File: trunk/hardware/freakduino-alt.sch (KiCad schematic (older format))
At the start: 10 parts, among them U6 ATMEGA328-QFP32

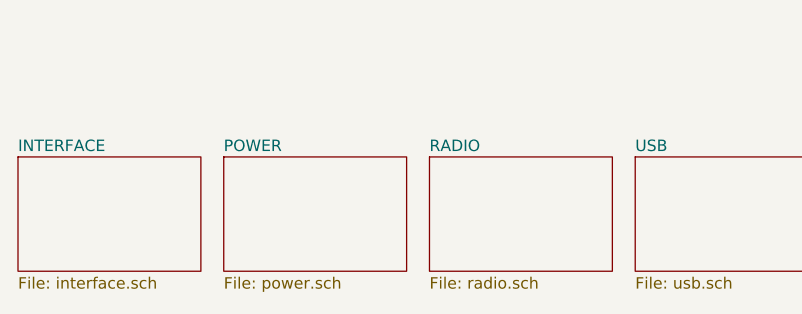
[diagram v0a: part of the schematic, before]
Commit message: CHANGING to -ALT files form this point onwards ...
Due to a number of changes from the original Freakduino design, I'm now
continuing my design in the freakduino-alt project, leaving a copy of the 
original work in the files without -alt.

The single shre/ folder (freakduino.lib, etc) will contain components,
and 3D modules for both versions.
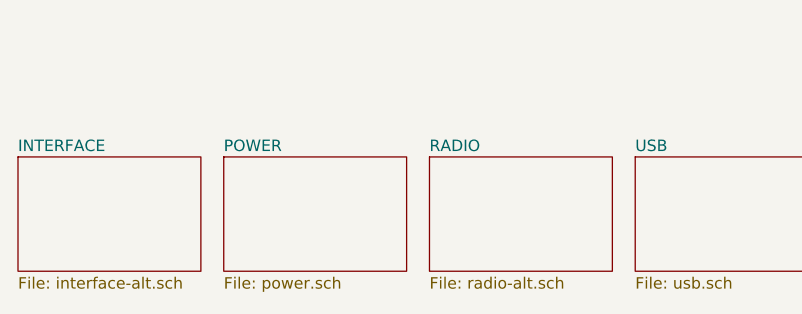
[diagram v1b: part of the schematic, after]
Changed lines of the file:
@@
 U 51E37E38
 F0 "RADIO" 50
-F1 "radio.sch" 50
+F1 "radio-alt.sch" 50
 $EndSheet
 $Sheet
@@
 U 51E6502D
 F0 "INTERFACE" 50
-F1 "interface.sch" 50
+F1 "interface-alt.sch" 50
 $EndSheet
 $EndSCHEMATC

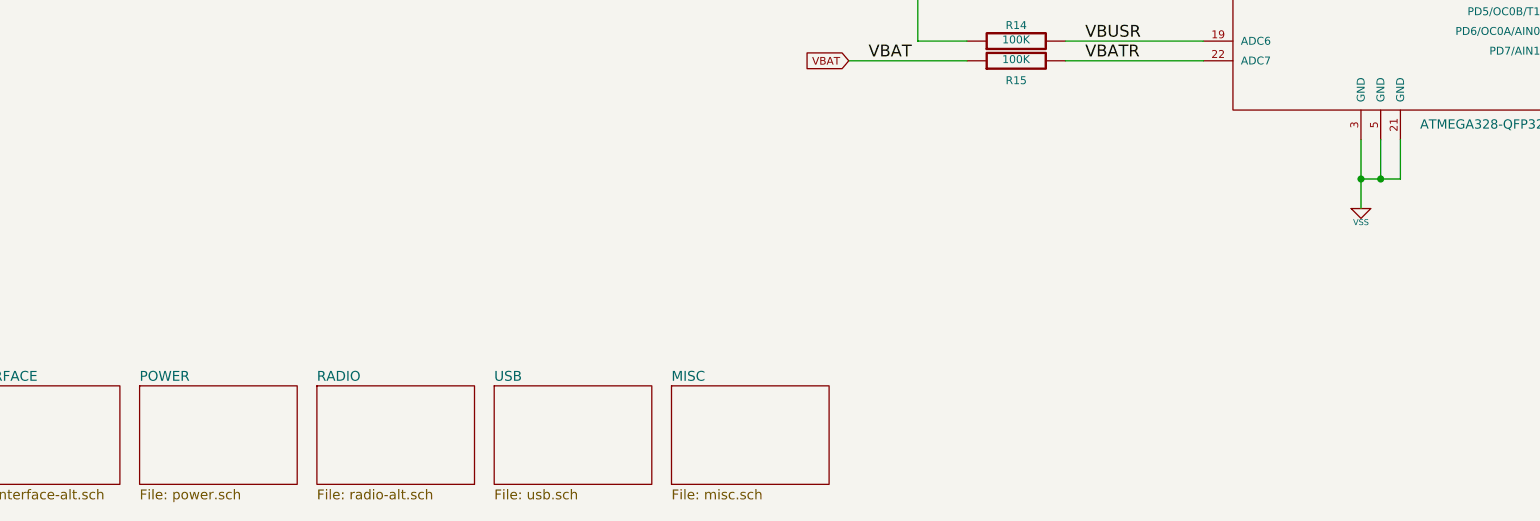
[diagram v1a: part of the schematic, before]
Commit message: Re-worked power supply boost circuit around an availabel part. Footprint and 3D package added for same.
Fixed multiple DRC errors with default KiCAD parts (saved in local 
library.)

Routed power boost circuit, paying attention to maximum GND/VSS 
shielding.

Set up fills for 50ohm (approx.) traces around radio chip and rest of 
board, both sides.

Updated BOM to reflect latest component changes.
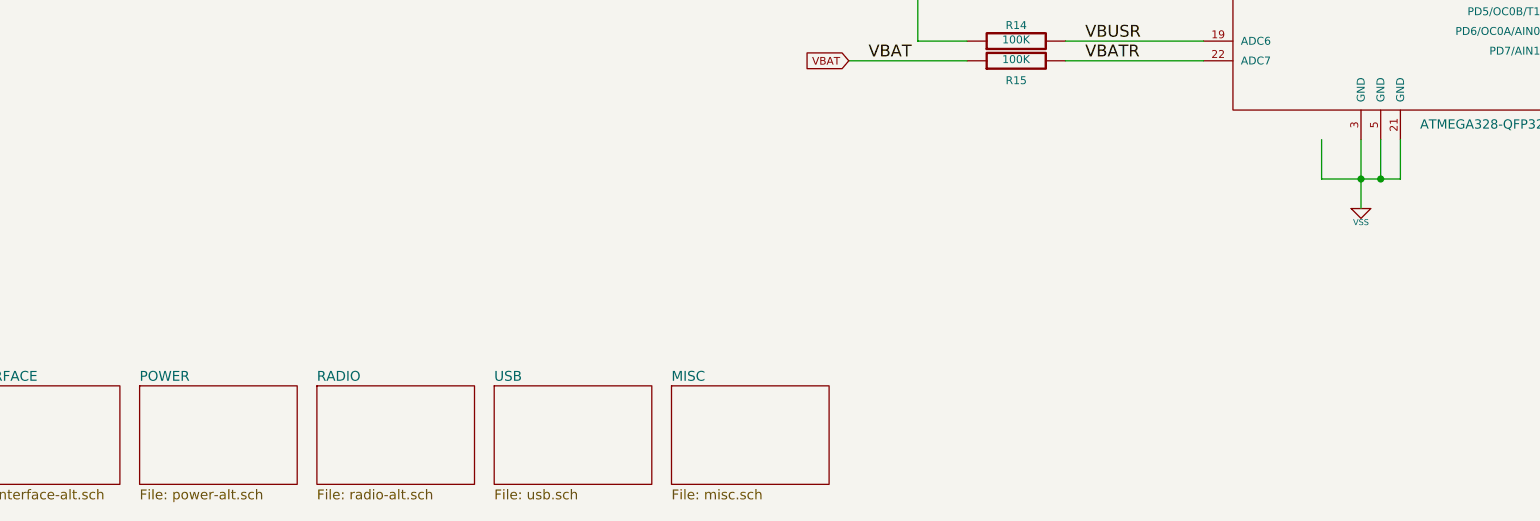
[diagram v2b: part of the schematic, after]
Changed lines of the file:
@@
 LIBS:contrib
 LIBS:valves
-LIBS:freakduino-cache
+LIBS:freakduino-alt-cache
 EELAYER 27 0
 EELAYER END
@@
 U 51E2B7E8
 F0 "POWER" 50
-F1 "power.sch" 50
+F1 "power-alt.sch" 50
 $EndSheet
 $Sheet
@@
 	7800 5900 7800 6100
 Wire Wire Line
-	7700 6100 7900 6100
+	7500 6100 7900 6100
 Connection ~ 7700 6100
 Wire Wire Line
@@
 F1 "interface-alt.sch" 50
 $EndSheet
+Wire Wire Line
+	7500 5900 7500 6100
 $EndSCHEMATC
